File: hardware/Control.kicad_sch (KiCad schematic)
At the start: 20 parts, among them J10 Conn_01x03, J11 Conn_01x03, J12 Conn_01x03, J13 Conn_01x03, J14 Conn_01x03, J15 Conn_01x03, J16 Conn_01x03, J17 Conn_01x03, J18 Conn_01x03, J19 Conn_01x03, J20 Conn_01x03, J21 Conn_01x03, J7 Conn_01x06, SW2 SW_Push, SW3 SW_Push

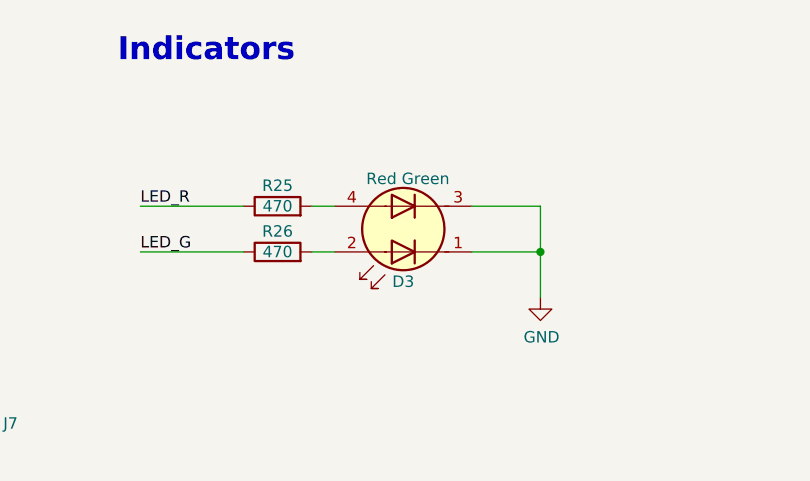
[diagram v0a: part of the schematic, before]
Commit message: fix: unavailable components
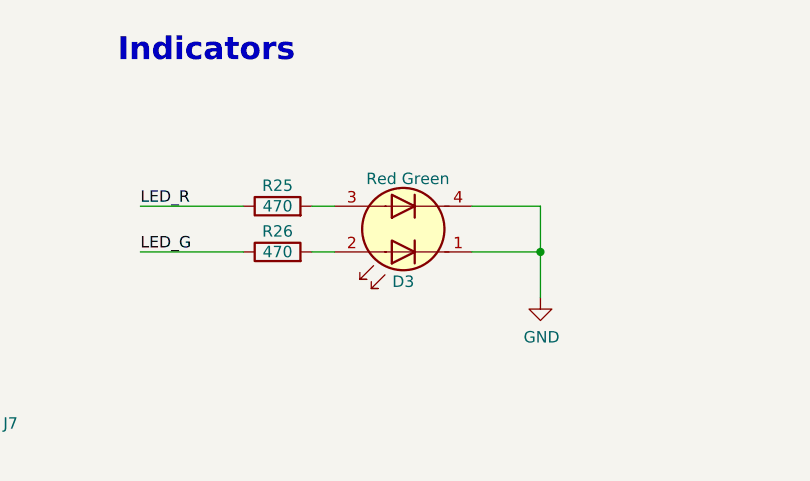
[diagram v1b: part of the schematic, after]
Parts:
- SW2, SW3: JLCPCB Part # C2689510 -> C139797; MPN PTS815SJM250SMTRLFS -> SKRPACE010; Manufacturer C&K -> ALPSALPINE
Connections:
- net GND: now also D3.4 (K2); no longer D3.3 (K2)
- net at R25.2: now also D3.3 (A2); no longer D3.4 (A2)
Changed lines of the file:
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@@
 			)
 		)
-		(property "Datasheet" "https://jlcpcb.com/api/file/downloadByFileSystemAccessId/8588902979558912000"
+		(property "Datasheet" "https://jlcpcb.com/api/file/downloadByFileSystemAccessId/8588899859952226304"
 			(at 52.07 38.1 0)
 			(effects
@@
 			)
 		)
-		(property "Description" "-20℃~+70℃ 1.8N 12V 50mA IP40 J-Lead Oval Button SPST-NO Surface Mount,Vertical SMD,3.2x4.2mm Tactile Switches ROHS"
+		(property "Description" "16V 2.5mm 3.2mm 4.2mm 50mA Oval Button SPST Surface Mount,Vertical SMD-4P,4.2x3.2mm Tactile Switches ROHS"
 			(at 52.07 43.18 0)
 			(effects
@@
 			)
 		)
-		(property "MPN" "PTS815SJM250SMTRLFS"
+		(property "MPN" "SKRPACE010"
 			(at 52.07 43.18 0)
 			(effects
@@
 			)
 		)
-		(property "Manufacturer" "C&K"
+		(property "Manufacturer" "ALPSALPINE"
 			(at 52.07 43.18 0)
 			(effects
@@
 			)
 		)
-		(property "JLCPCB Part #" "C2689510"
+		(property "JLCPCB Part #" "C139797"
 			(at 52.07 43.18 0)
 			(effects
@@
 			)
 		)
-		(property "Datasheet" "https://jlcpcb.com/api/file/downloadByFileSystemAccessId/8588902979558912000"
+		(property "Datasheet" "https://jlcpcb.com/api/file/downloadByFileSystemAccessId/8588899859952226304"
 			(at 52.07 102.87 0)
 			(effects
@@
 			)
 		)
-		(property "Description" "-20℃~+70℃ 1.8N 12V 50mA IP40 J-Lead Oval Button SPST-NO Surface Mount,Vertical SMD,3.2x4.2mm Tactile Switches ROHS"
+		(property "Description" "16V 2.5mm 3.2mm 4.2mm 50mA Oval Button SPST Surface Mount,Vertical SMD-4P,4.2x3.2mm Tactile Switches ROHS"
 			(at 52.07 107.95 0)
 			(effects
@@
 			)
 		)
-		(property "MPN" "PTS815SJM250SMTRLFS"
+		(property "MPN" "SKRPACE010"
 			(at 52.07 107.95 0)
 			(effects
@@
 			)
 		)
-		(property "Manufacturer" "C&K"
+		(property "Manufacturer" "ALPSALPINE"
 			(at 52.07 107.95 0)
 			(effects
@@
 			)
 		)
-		(property "JLCPCB Part #" "C2689510"
+		(property "JLCPCB Part #" "C139797"
 			(at 52.07 107.95 0)
 			(effects

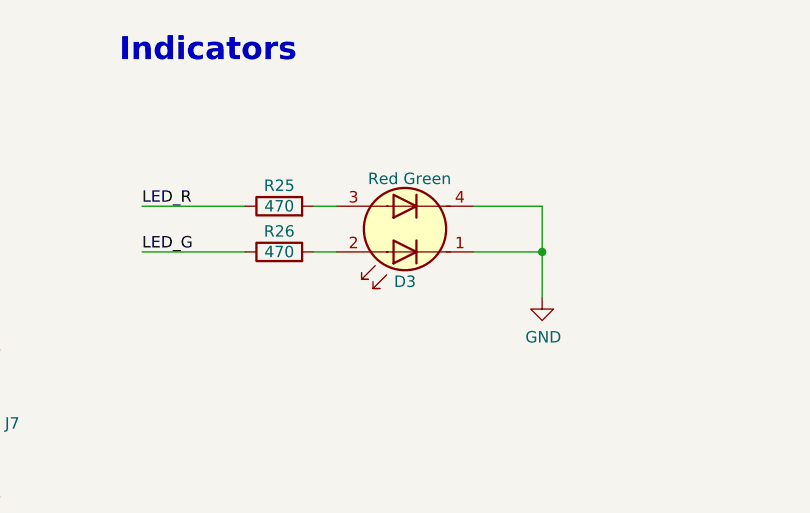
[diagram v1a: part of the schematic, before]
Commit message: feat: replace status LED
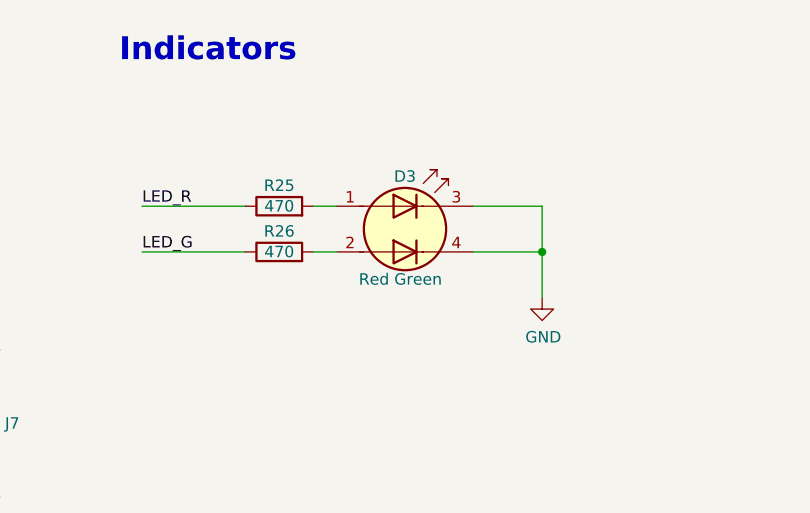
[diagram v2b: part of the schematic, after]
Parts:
- D3: footprint LED_SMD:LED_LiteOn_LTST-C235KGKRKT -> LED_SMD:LED_LiteOn_LTST-C295K_1.6x0.8mm; symbol Device:LED_Dual_KAKA -> Device:LED_Dual_AAKK; JLCPCB Part # C125110 -> C364568; MPN LTST-C235KGKRKT -> LTST-C295KGKRKT
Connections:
- net GND: now also D3.3 (K1); no longer D3.1 (K1)
- net at R25.2: now also D3.1 (A1); no longer D3.3 (A2)
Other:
- moved on the sheet: D3
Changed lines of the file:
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@@
 	)
 	(symbol
-		(lib_id "Device:LED_Dual_KAKA")
-		(at 121.92 45.72 180)
+		(lib_id "Device:LED_Dual_AAKK")
+		(at 121.92 45.72 0)
 		(unit 1)
 		(exclude_from_sim no)
@@
 		(dnp no)
 		(property "Reference" "D3"
-			(at 121.92 51.562 0)
+			(at 121.92 39.878 0)
 			(effects
 				(font
@@
 		)
 		(property "Value" "Red Green"
-			(at 122.428 40.132 0)
+			(at 121.412 51.308 0)
 			(effects
 				(font
@@
 			)
 		)
-		(property "Footprint" "LED_SMD:LED_LiteOn_LTST-C235KGKRKT"
-			(at 121.158 45.72 0)
+		(property "Footprint" "LED_SMD:LED_LiteOn_LTST-C295K_1.6x0.8mm"
+			(at 122.682 45.72 0)
 			(effects
 				(font
@@
 			)
 		)
-		(property "Datasheet" "https://jlcpcb.com/api/file/downloadByFileSystemAccessId/8588894590669082624"
-			(at 121.158 45.72 0)
+		(property "Datasheet" "https://jlcpcb.com/api/file/downloadByFileSystemAccessId/8588931534900908032"
+			(at 122.682 45.72 0)
 			(effects
 				(font
@@
 			)
 		)
-		(property "Description" "-30℃~+85℃ 130° 2V 571nm 574nm 75mW Red, Yellow Green Reverse Mount Water Clear SMD-4P,3.2x1.6mm LED Indication - Discrete ROHS"
+		(property "Description" "-30℃~+85℃ 130° 20mA 2V 45mcd 571nm 574nm 75mW Red, Yellow Green Water Clear SMD-4P,1.6x0.8mm LED Indication - Discrete ROHS"
 			(at 121.92 45.72 0)
 			(effects
@@
 			)
 		)
-		(property "MPN" "LTST-C235KGKRKT"
+		(property "MPN" "LTST-C295KGKRKT"
 			(at 121.92 45.72 0)
 			(effects
@@
 			)
 		)
-		(property "JLCPCB Part #" "C125110"
+		(property "JLCPCB Part #" "C364568"
 			(at 121.92 45.72 0)
 			(effects

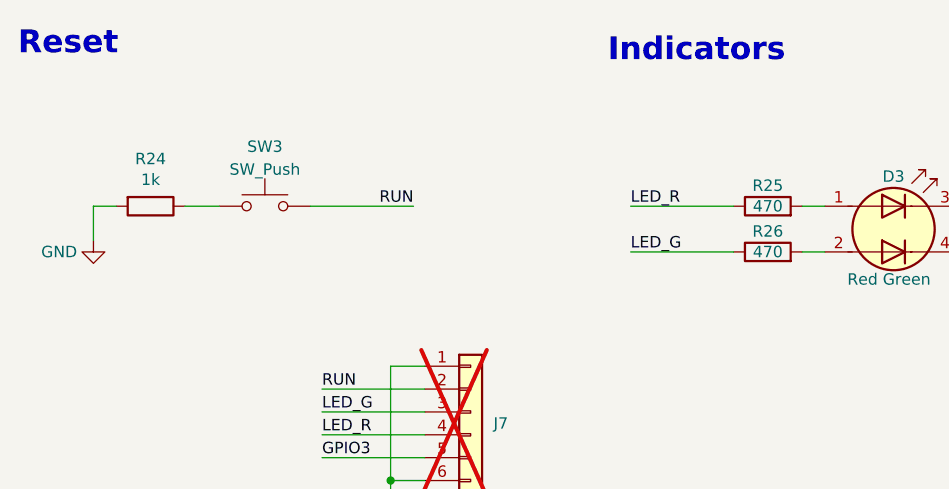
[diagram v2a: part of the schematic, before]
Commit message: fix: status LED resistor value
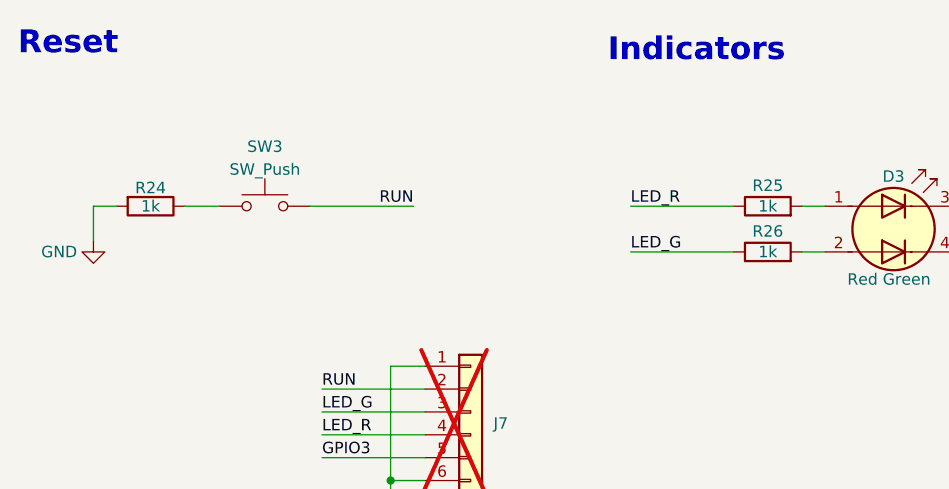
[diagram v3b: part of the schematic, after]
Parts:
- R25, R26: value 470 -> 1k; JLCPCB Part # C606172 -> C106235; MPN RC0402FR-7W470RL -> RC0402FR-071KL
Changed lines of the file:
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@@
 			)
 		)
-		(property "Value" "470"
+		(property "Value" "1k"
 			(at 107.95 43.18 90)
 			(effects
@@
 			)
 		)
-		(property "Datasheet" "https://wmsc.lcsc.com/wmsc/upload/file/pdf/v2/lcsc/2006112330_YAGEO-RC0402FR-7W470RL_C606172.pdf"
+		(property "Datasheet" "https://jlcpcb.com/api/file/downloadByFileSystemAccessId/8588898674722553856"
 			(at 107.95 43.18 0)
 			(effects
@@
 			)
 		)
-		(property "Description" "125mW Thick Film Resistors 50V ±100ppm/℃ ±1% 470Ω 0402 Chip Resistor - Surface Mount ROHS"
+		(property "Description" "-55℃~+155℃ 1kΩ 50V 62.5mW Thick Film Resistor ±1% ±100ppm/℃ 0402 Chip Resistor - Surface Mount ROHS"
 			(at 107.95 43.18 0)
 			(effects
@@
 			)
 		)
-		(property "MPN" "RC0402FR-7W470RL"
+		(property "MPN" "RC0402FR-071KL"
 			(at 107.95 43.18 90)
 			(effects
@@
 			)
 		)
-		(property "JLCPCB Part #" "C606172"
+		(property "Manufacturer" "YAGEO"
 			(at 107.95 43.18 90)
 			(effects
@@
 			)
 		)
-		(property "Manufacturer" "YAGEO"
+		(property "JLCPCB Part #" "C106235"
 			(at 107.95 43.18 90)
 			(effects
@@
 			)
 		)
-		(property "Value" "470"
+		(property "Value" "1k"
 			(at 107.95 48.26 90)
 			(effects
@@
 			)
 		)
-		(property "Datasheet" "https://wmsc.lcsc.com/wmsc/upload/file/pdf/v2/lcsc/2006112330_YAGEO-RC0402FR-7W470RL_C606172.pdf"
+		(property "Datasheet" "https://jlcpcb.com/api/file/downloadByFileSystemAccessId/8588898674722553856"
 			(at 107.95 48.26 0)
 			(effects
@@
 			)
 		)
-		(property "Description" "125mW Thick Film Resistors 50V ±100ppm/℃ ±1% 470Ω 0402 Chip Resistor - Surface Mount ROHS"
+		(property "Description" "-55℃~+155℃ 1kΩ 50V 62.5mW Thick Film Resistor ±1% ±100ppm/℃ 0402 Chip Resistor - Surface Mount ROHS"
 			(at 107.95 48.26 0)
 			(effects
@@
 			)
 		)
-		(property "MPN" "RC0402FR-7W470RL"
+		(property "MPN" "RC0402FR-071KL"
 			(at 107.95 48.26 90)
 			(effects
@@
 			)
 		)
-		(property "JLCPCB Part #" "C606172"
+		(property "Manufacturer" "YAGEO"
 			(at 107.95 48.26 90)
 			(effects
@@
 			)
 		)
-		(property "Manufacturer" "YAGEO"
+		(property "JLCPCB Part #" "C106235"
 			(at 107.95 48.26 90)
 			(effects
@@
 		(dnp no)
 		(property "Reference" "R24"
-			(at 39.37 37.9222 90)
+			(at 39.37 41.148 90)
 			(effects
 				(font
@@
 		)
 		(property "Value" "1k"
-			(at 39.37 40.2336 90)
-			(effects
-				(font
+			(at 39.37 43.18 90)
+			(effects
+				(font
